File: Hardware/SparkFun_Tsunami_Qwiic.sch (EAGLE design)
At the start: 194 parts, among them J1 VDC-IN, J10 TRIG2, J11 TRIG1, J14 AUDIO I/O, J15 MIDI, J16 USB-C, J17 AGND, J2 GND-IN, J3 DEBUG, J4 QWIIC, J6 3.3VA, J7 3.3V, J8 PLAYING, J9 CORTEX_JTAG_DEBUG_PTH_NS, Q1 3.1A/30V/105mΩ, U1 LM1117, U3 ATSAMS70N20A-AN, U4 LMV324, U5 LM1117, U6 6N138M, U7 ADAU1328, U8 SN74AHC1G125, Y1 11.2896 MHz

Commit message: Single buffer gate change
drop in replacement for U8 single buffer IC, with new PROD_ID
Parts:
- U8: value SN74AHC1G125 -> 74AHC1G125W5-7; device SparkFun-IC-Logic:74AHC1G125D -> SparkFun-IC-Logic:741G12574AHC1G125W5-7
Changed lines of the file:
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@@
 <part name="SUPPLY16" library="SparkFun-PowerSymbols" deviceset="V_USB" device="" value="V_USB"/>
 <part name="SUPPLY17" library="SparkFun-PowerSymbols" deviceset="VIN" device=""/>
-<part name="U8" library="SparkFun-IC-Logic" deviceset="74*1G125" device="D" technology="AHC" value="SN74AHC1G125"/>
+<part name="U8" library="SparkFun-IC-Logic" deviceset="74*1G125" device="74AHC1G125W5-7" value="74AHC1G125W5-7"/>
 <part name="SUPPLY19" library="SparkFun-PowerSymbols" deviceset="3.3V" device=""/>
 <part name="GND6" library="SparkFun-PowerSymbols" deviceset="DGND" device=""/>

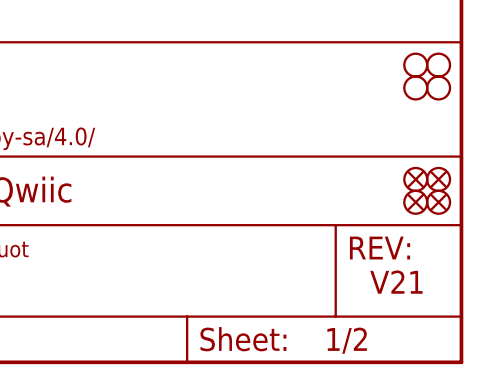
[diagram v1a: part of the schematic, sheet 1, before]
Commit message: Swap 11MHz crystal for smaller package (3.2x2.5mm)
-also bumped version in bottom copper and SCH
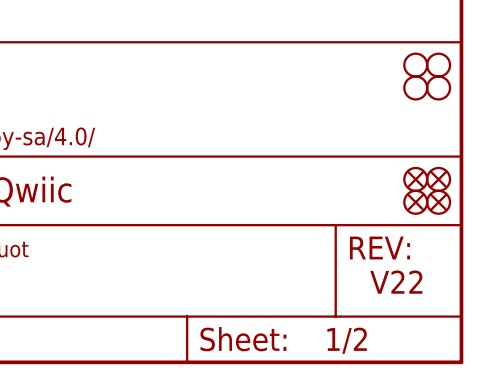
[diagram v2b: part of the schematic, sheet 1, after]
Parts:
- Y1: device SparkFun-Clocks:CRYSTAL-11.2896 -> SparkFun-Clocks:CRYSTAL-11.28963.2X2.5
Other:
- note added: "V22"
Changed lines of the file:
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@@
 <part name="J10" library="SparkFun-Connectors" deviceset="CONN_08X2" device="_NOSILK" value="TRIG2"/>
 <part name="J11" library="SparkFun-Connectors" deviceset="CONN_08X2" device="_NOSILK" value="TRIG1"/>
-<part name="Y1" library="SparkFun-Clocks" deviceset="CRYSTAL-11.2896" device="" value="11.2896 MHz"/>
+<part name="Y1" library="SparkFun-Clocks" deviceset="CRYSTAL-11.2896" device="3.2X2.5" value="11.2896 MHz"/>
 <part name="C37" library="SparkFun-Capacitors" deviceset="0.1UF" device="-0402T-16V-10%" value="0.1uF"/>
 <part name="C38" library="SparkFun-Capacitors" deviceset="1.0UF" device="-0402T-16V-10%" value="1.0uF"/>
@@
 <wire x1="431.8" y1="88.9" x2="330.2" y2="88.9" width="0.1524" layer="97" style="shortdash"/>
 <text x="348.996" y="11.684" size="1.778" layer="94" font="vector">Jamie Robertson, Byron Jacquot</text>
-<text x="421.64" y="7.62" size="2.54" layer="94" font="vector">V21</text>
+<text x="421.64" y="7.62" size="2.54" layer="94" font="vector">V22</text>
 <text x="244.348" y="262.128" size="1.778" layer="97" font="vector">Near each VDDCORE pin</text>
 <text x="211.328" y="262.128" size="1.778" layer="97" font="vector">Near each VDDIO pin</text>

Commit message: Test points changed to larger size
-8 test points updated. Note, these used to be the small 15mil drill hit pth/via style test points. They are now the largest SMD pad style. Note, I also kept a via in the center point of all the test points, this was necessary to keep routing adjustments to a minimum and it will also help with pogo pin centering.
-Bumped version to v23 in BRD and both sheets of SCH
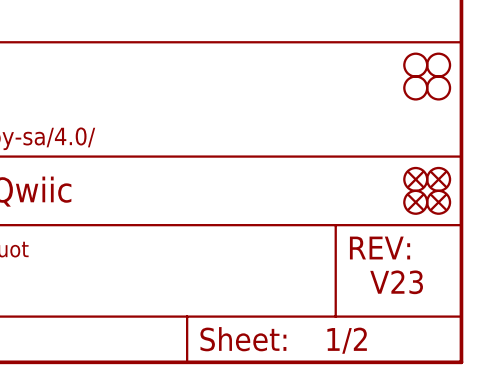
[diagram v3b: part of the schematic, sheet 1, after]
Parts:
- TP1, TP2, TP4, TP5, TP6, TP7, TP8, TP9: device SparkFun-Connectors:TEST-POINTTP_15TH_THRU -> SparkFun-Connectors:TEST-POINT3X5
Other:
- note added: "V23"
- note removed: "V21"
- note removed: "V22"
